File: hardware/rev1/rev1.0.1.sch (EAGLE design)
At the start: 42 parts, among them Q1 MOSFET-NCHANNEL-IRLR3705ZPBF, Q2 MOSFET-PCHANNEL, Q3 MOSFET-NCHANNELBSS138, U1 ATMEGA168-AU, U2 5v, U3 74AHC1G04DBV, Y1 16MHz

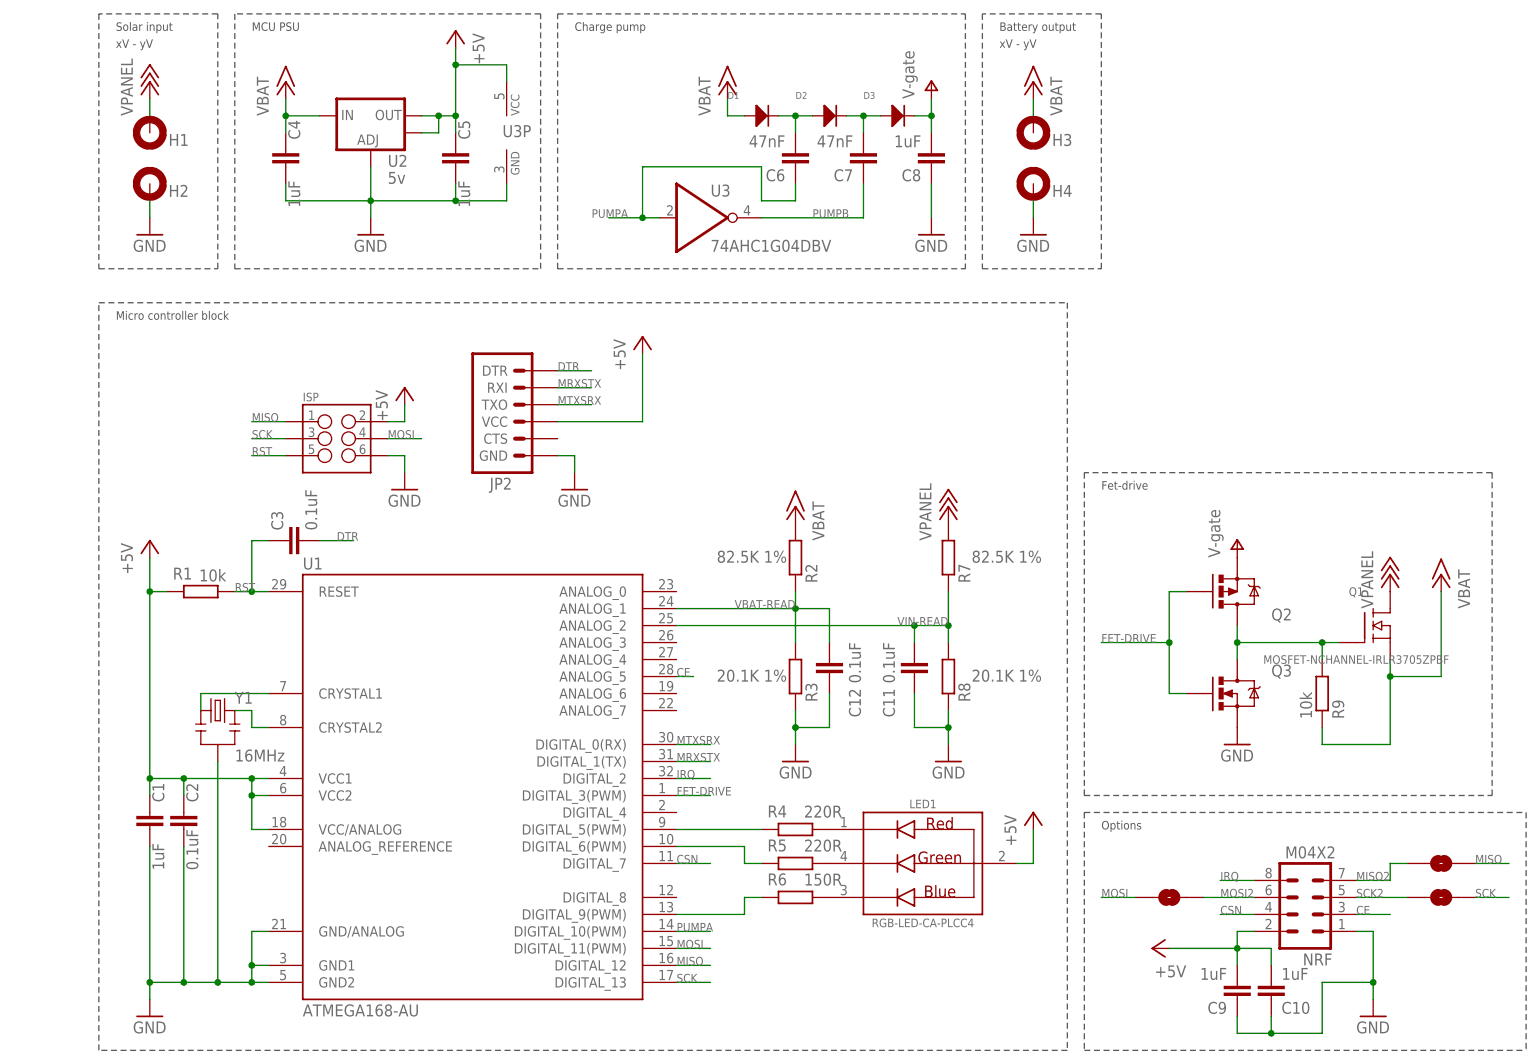
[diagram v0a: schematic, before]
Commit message: Propperly filtered AVCC
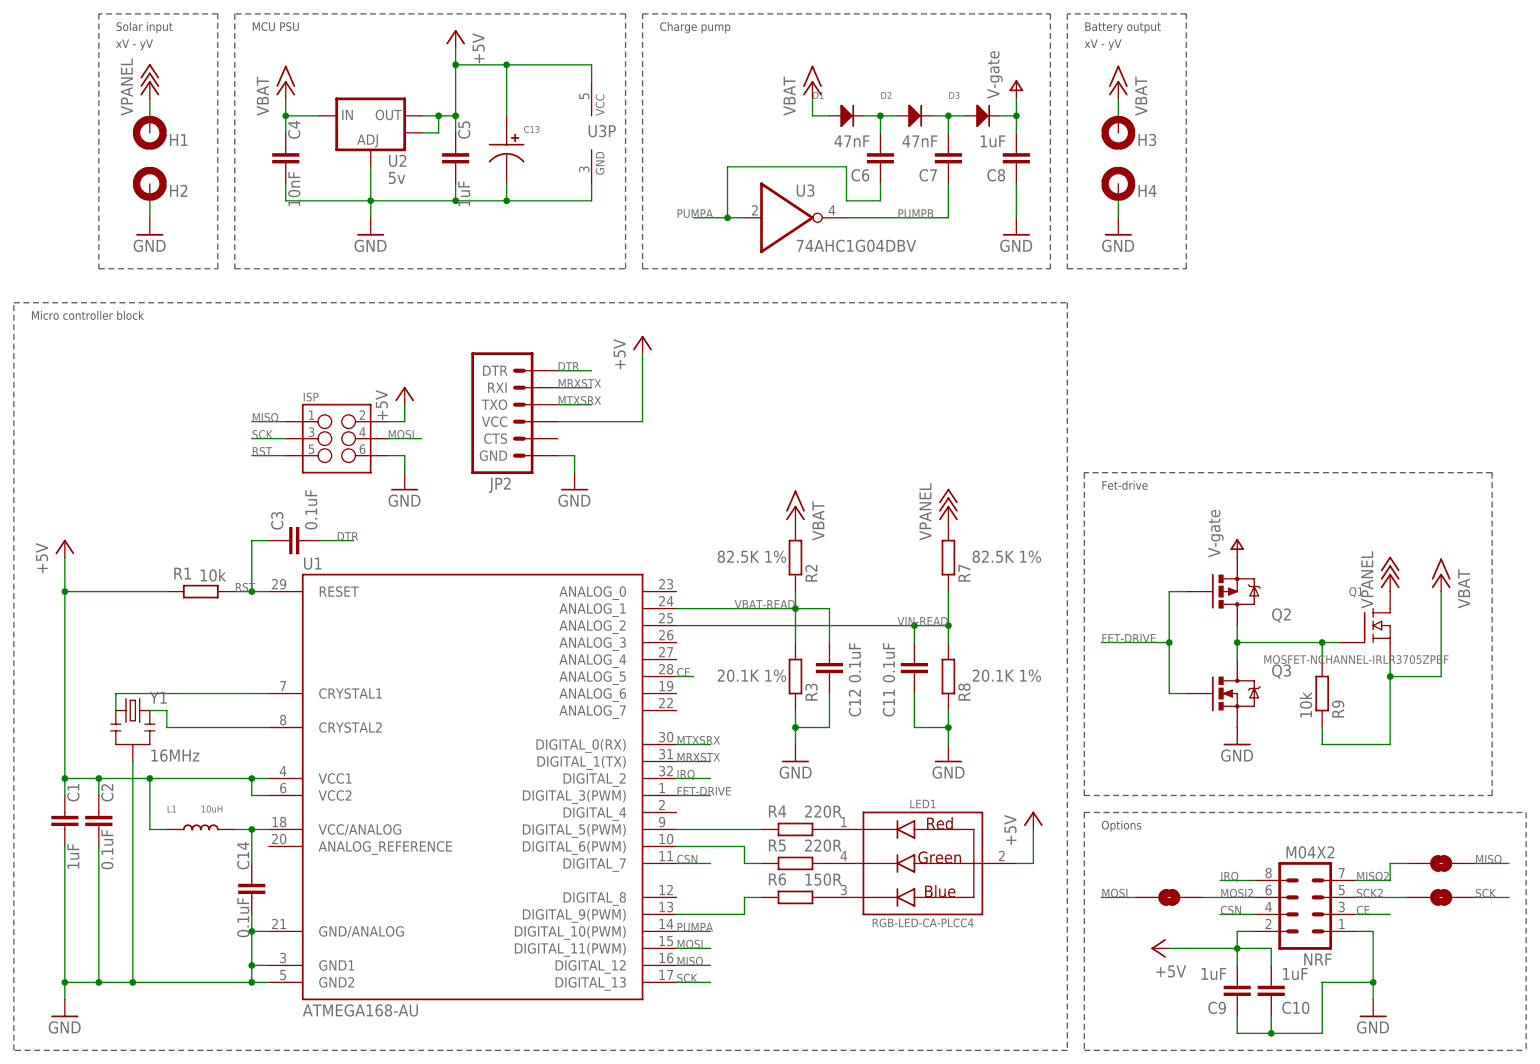
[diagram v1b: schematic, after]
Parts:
- added C13: (no value), MF_Passives:CAPACITOR_P_4MM
- added C14: 0.1uF, resistor:C-EUC0603K
- added L1: 10uH, MF_Passives:INDUCTOR_1210
- C4: value 1uF -> 10nF
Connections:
- new net N$14: C14.1, L1.P$2, U1.VCC/ANALOG
- net +5V: now also C13.P$1, L1.P$1; no longer U1.VCC/ANALOG
- net GND: now also C13.P$2, C14.2
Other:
- moved on the sheet: C1, C2, C6, C7, C8, D1, D2, D3, H3, H4, U3, U3P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
